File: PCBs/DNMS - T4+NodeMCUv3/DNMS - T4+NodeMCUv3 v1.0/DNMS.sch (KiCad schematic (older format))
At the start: 15 parts, among them J1 Conn_02x03_Odd_Even, J2 Conn_01x02, J3 Conn_01x04, J4 Conn_01x05, U2 NodeMCU V3, U3 Teensy4.0

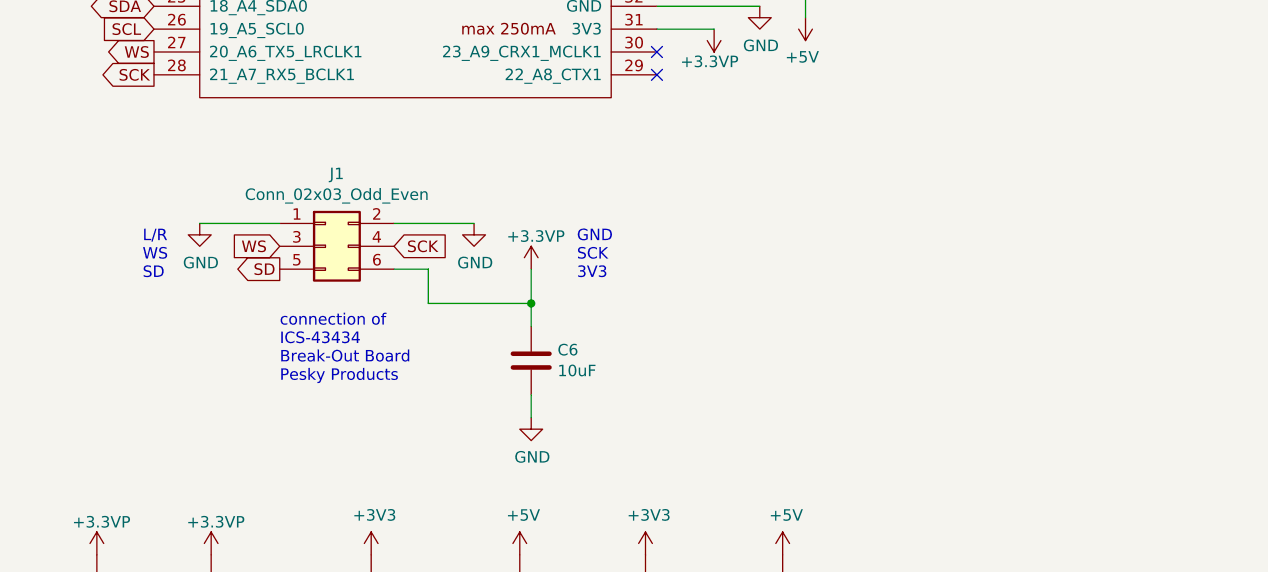
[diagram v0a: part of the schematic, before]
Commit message: change connector to mic to molex pico-ezmate
move other connectors around
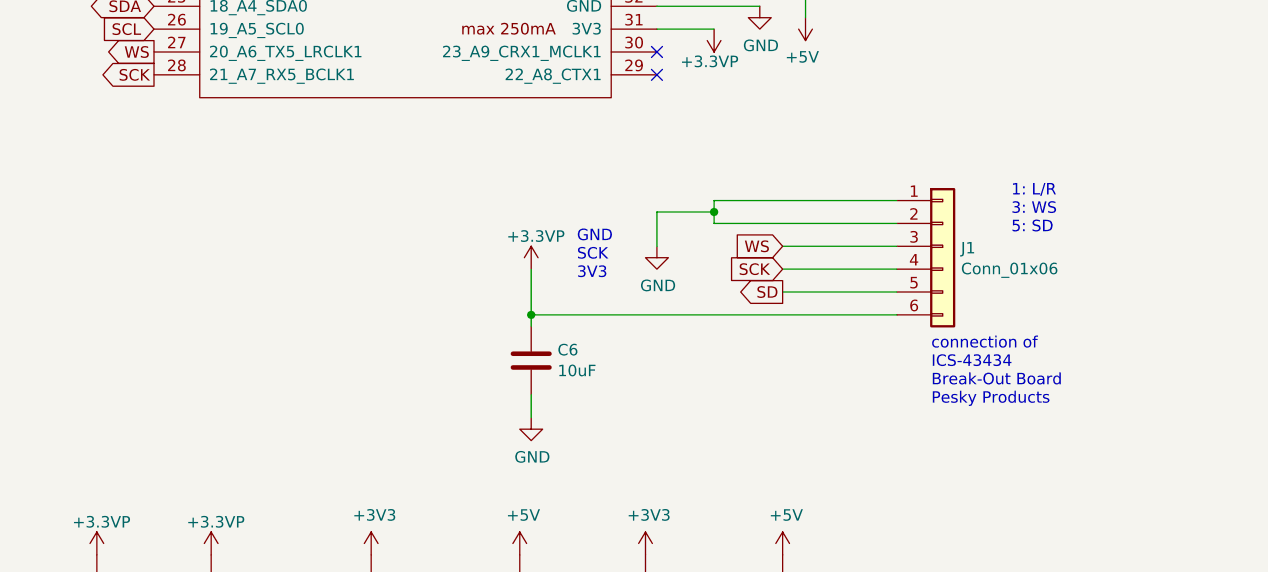
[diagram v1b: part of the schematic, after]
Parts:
- removed J1: Conn_02x03_Odd_Even, Connector_PinHeader_2.54mm:PinHeader_2x03_P2.54mm_Vertical, symbol Connector_Generic:Conn_02x03_Odd_Even
- added J1: Conn_01x06, Connector_Molex:Molex_Pico-EZmate_78171-0005_1x05-1MP_P1.20mm_Vertical, symbol Connector_Generic:Conn_01x06
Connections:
- net +3.3VP: now also J1.6 (Pin_6)
- net GND: now also J1.1 (Pin_1), J1.2 (Pin_2)
- net SCK: now also J1.4 (Pin_4)
- net SD: now also J1.5 (Pin_5)
- net WS: now also J1.3 (Pin_3)
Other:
- note added: "1: L/R\n3: WS\n5: SD"
- note removed: "L/R\nWS\nSD"
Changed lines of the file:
@@
 Text Notes 4800 3250 0    50   ~ 0
 Jumper\nVUSB nach VIN
-Text Notes 1350 4700 0    50   ~ 0
-L/R\nWS\nSD
-Text Notes 1950 5150 0    50   ~ 0
+Text Notes 5150 4500 0    50   ~ 0
+1: L/R\n3: WS\n5: SD
+Text Notes 4800 5250 0    50   ~ 0
 connection of\nICS-43434\nBreak-Out Board\nPesky Products
 Text Notes 3250 4700 0    50   ~ 0
@@
 Text GLabel 9350 4500 0    50   Input ~ 0
 SCL
-Text GLabel 1950 4550 0    50   Input ~ 0
-WS
-Text GLabel 1950 4650 0    50   Output ~ 0
-SD
-Text GLabel 2450 4550 2    50   Input ~ 0
-SCK
-Wire Wire Line
-	1950 4450 1600 4450
-Wire Wire Line
-	2450 4450 2800 4450
-$Comp
-L power:GND #PWR0126
-U 1 1 5D6C3101
-P 1600 4450
-F 0 "#PWR0126" H 1600 4200 50  0001 C CNN
-F 1 "GND" H 1605 4277 50  0000 C CNN
-F 2 "" H 1600 4450 50  0001 C CNN
-F 3 "" H 1600 4450 50  0001 C CNN
-	1    1600 4450
-	1    0    0    -1
-$EndComp
-$Comp
-L power:GND #PWR0127
-U 1 1 5D6C35EC
-P 2800 4450
-F 0 "#PWR0127" H 2800 4200 50  0001 C CNN
-F 1 "GND" H 2805 4277 50  0000 C CNN
-F 2 "" H 2800 4450 50  0001 C CNN
-F 3 "" H 2800 4450 50  0001 C CNN
-	1    2800 4450
-	1    0    0    -1
-$EndComp
-Wire Wire Line
-	2450 4650 2600 4650
-Wire Wire Line
-	2600 4650 2600 4800
-Wire Wire Line
-	2600 4800 3050 4800
-Wire Wire Line
-	3050 4800 3050 4650
 $Comp
 L power:+3.3VP #PWR0128
@@
 	10000 2700 9700 2700
 $Comp
-L Connector_Generic:Conn_02x03_Odd_Even J1
-U 1 1 5E455872
-P 2150 4550
-F 0 "J1" H 2200 4867 50  0000 C CNN
-F 1 "Conn_02x03_Odd_Even" H 2200 4776 50  0000 C CNN
-F 2 "Connector_PinHeader_2.54mm:PinHeader_2x03_P2.54mm_Vertical" H 2150 4550 50  0001 C CNN
-F 3 "~" H 2150 4550 50  0001 C CNN
-	1    2150 4550
-	1    0    0    -1
-$EndComp
-$Comp
 L Device:C C4
 U 1 1 5E4DAB70
@@
 $EndComp
 Wire Wire Line
-	3050 4900 3050 4800
-Connection ~ 3050 4800
+	3050 4900 3050 4850
 Wire Wire Line
 	3050 5200 3050 5300
@@
 	1    0    0    -1
 $EndComp
+$Comp
+L Connector_Generic:Conn_01x06 J1
+U 1 1 5E508C40
+P 4850 4550
+F 0 "J1" H 4930 4542 50  0000 L CNN
+F 1 "Conn_01x06" H 4930 4451 50  0000 L CNN
+F 2 "Connector_Molex:Molex_Pico-EZmate_78171-0005_1x05-1MP_P1.20mm_Vertical" H 4850 4550 50  0001 C CNN
+F 3 "~" H 4850 4550 50  0001 C CNN
+	1    4850 4550
+	1    0    0    -1
+$EndComp
+Wire Wire Line
+	4650 4350 3850 4350
+Wire Wire Line
+	4650 4450 3850 4450
+Wire Wire Line
+	3850 4350 3850 4400
+Wire Wire Line
+	3850 4400 3600 4400
+Wire Wire Line
+	3600 4400 3600 4550
+Connection ~ 3850 4400
+Wire Wire Line
+	3850 4400 3850 4450
+$Comp
+L power:GND #PWR0126
+U 1 1 5E512A7D
+P 3600 4550
+F 0 "#PWR0126" H 3600 4300 50  0001 C CNN
+F 1 "GND" H 3605 4377 50  0000 C CNN
+F 2 "" H 3600 4550 50  0001 C CNN
+F 3 "" H 3600 4550 50  0001 C CNN
+	1    3600 4550
+	1    0    0    -1
+$EndComp
+Wire Wire Line
+	3050 4850 4650 4850
+Connection ~ 3050 4850
+Wire Wire Line
+	4650 4550 4150 4550
+Wire Wire Line
+	4650 4650 4150 4650
+Wire Wire Line
+	4650 4750 4150 4750
+Text GLabel 4150 4550 0    50   Input ~ 0
+WS
+Text GLabel 4150 4650 0    50   Input ~ 0
+SCK
+Text GLabel 4150 4750 0    50   Output ~ 0
+SD
+Wire Wire Line
+	3050 4650 3050 4850
 $EndSCHEMATC

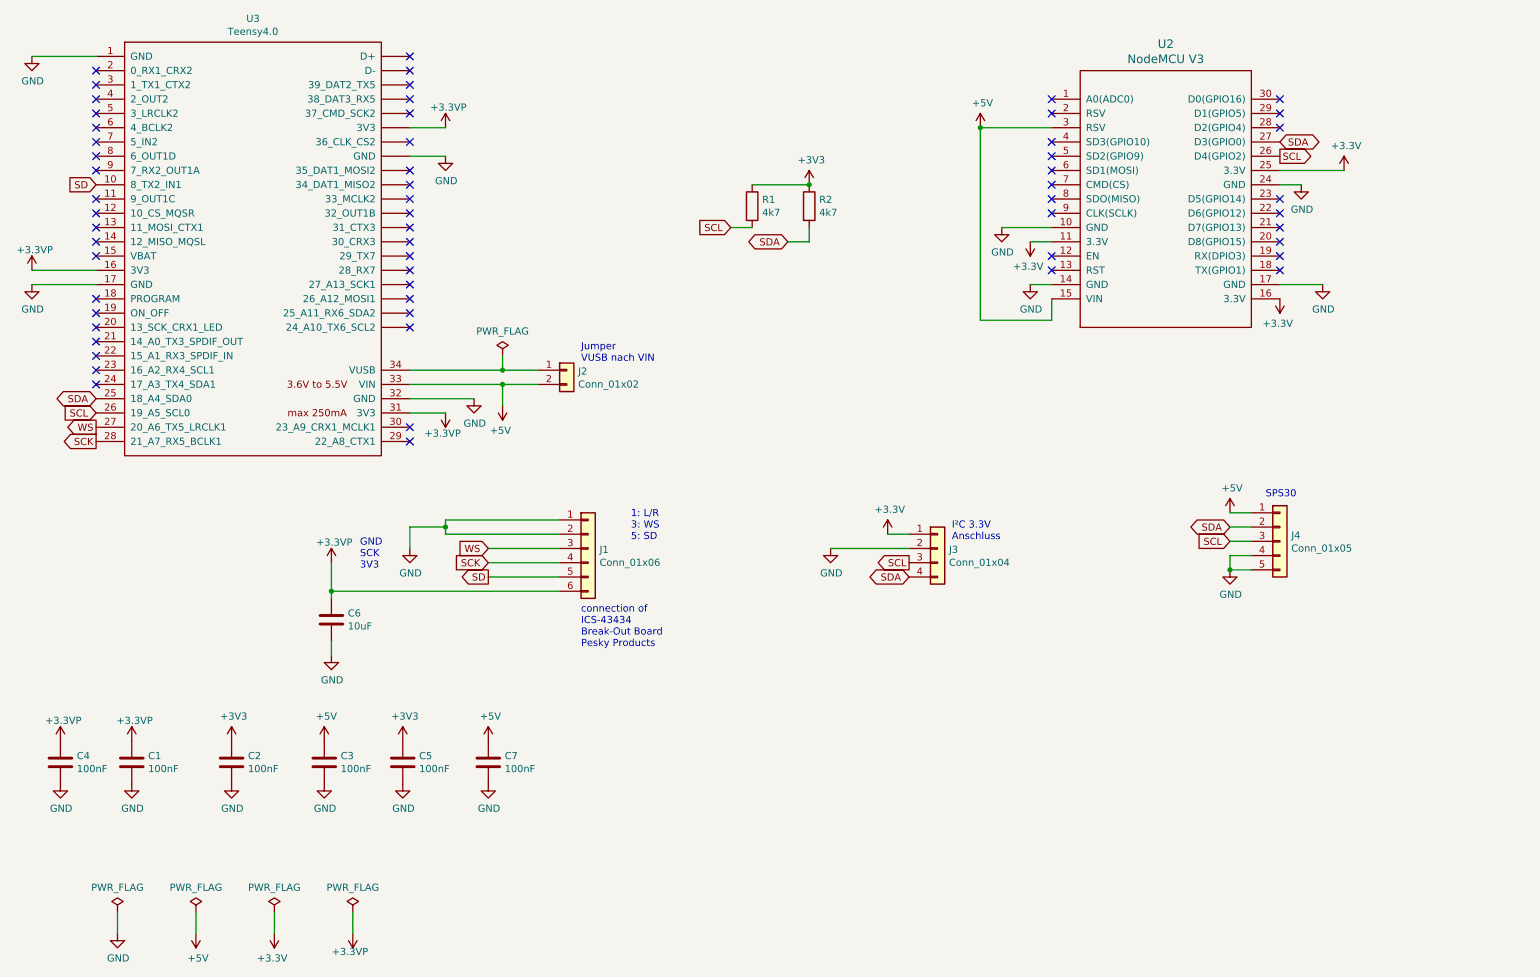
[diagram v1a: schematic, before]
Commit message: add 2.54mm connector headers next to pico ezmate connectors
for backwards compability

moved text around and cleaned design

added additional capcitors
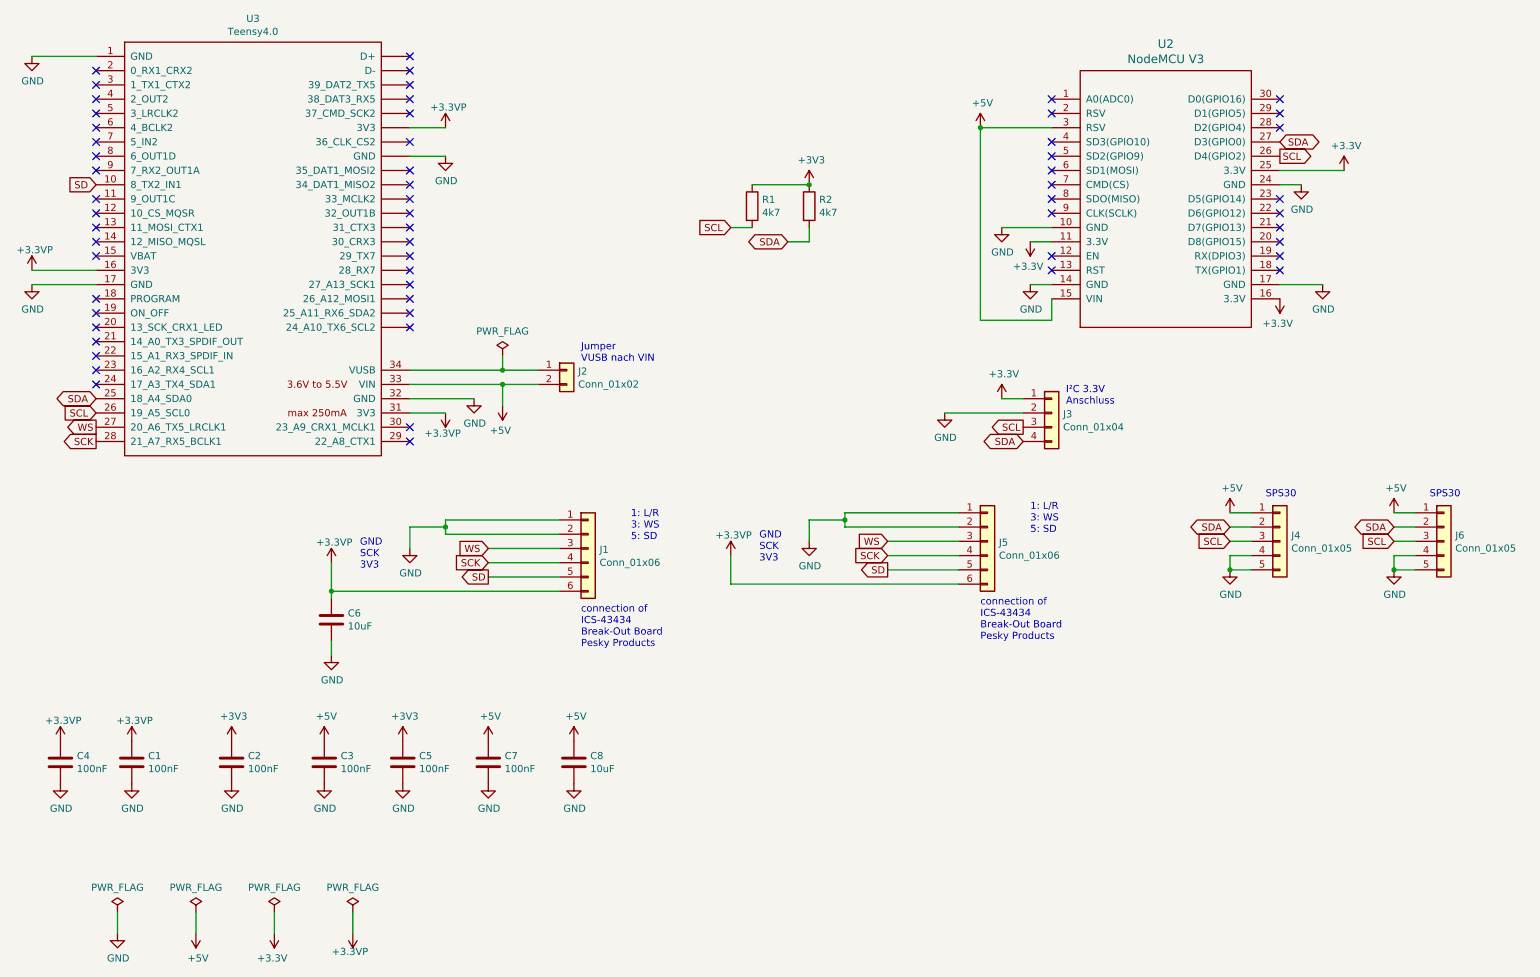
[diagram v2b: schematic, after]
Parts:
- added C8: 10uF, Capacitor_SMD:C_0805_2012Metric_Pad1.15x1.40mm_HandSolder, symbol Device:C
- added J5: Conn_01x06, Connector_PinHeader_2.54mm:PinHeader_1x06_P2.54mm_Vertical, symbol Connector_Generic:Conn_01x06
- added J6: Conn_01x05, Connector_PinHeader_2.54mm:PinHeader_1x05_P2.54mm_Vertical, symbol Connector_Generic:Conn_01x05
- J1: footprint Connector_Molex:Molex_Pico-EZmate_78171-0005_1x05-1MP_P1.20mm_Vertical -> Connector_Molex:molex_pico-ezmate_781715006_1x06_P1.20mm_Horizontal
- J4: footprint Connector_JST_ZH:JST_ZH_S5B-EH_1x05_P1.50mm_Horizontal -> Connector_Molex:Molex_Pico-EZmate_78171-0005_1x05-1MP_P1.20mm_Horizontal
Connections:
- net +3.3VP: now also J5.6 (Pin_6)
- net +5V: now also C8.1, J6.1 (Pin_1)
- net GND: now also C8.2, J5.1 (Pin_1), J5.2 (Pin_2), J6.4 (Pin_4), J6.5 (Pin_5)
- net SCK: now also J5.4 (Pin_4)
- net SCL: now also J6.3 (Pin_3)
- net SD: now also J5.5 (Pin_5)
- net SDA: now also J6.2 (Pin_2)
- net WS: now also J5.3 (Pin_3)
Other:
- moved on the sheet: J3
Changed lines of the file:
@@
 L Connector_Generic:Conn_01x04 J3
 U 1 1 5CFB9C02
-P 7300 4550
-F 0 "J3" H 7380 4542 50  0000 L CNN
-F 1 "Conn_01x04" H 7380 4451 50  0000 L CNN
-F 2 "Connector_PinHeader_2.54mm:PinHeader_1x04_P2.54mm_Vertical" H 7300 4550 50  0001 C CNN
-F 3 "~" H 7300 4550 50  0001 C CNN
-	1    7300 4550
+P 8100 3600
+F 0 "J3" H 8180 3592 50  0000 L CNN
+F 1 "Conn_01x04" H 8180 3501 50  0000 L CNN
+F 2 "Connector_PinHeader_2.54mm:PinHeader_1x04_P2.54mm_Vertical" H 8100 3600 50  0001 C CNN
+F 3 "~" H 8100 3600 50  0001 C CNN
+	1    8100 3600
 	1    0    0    -1
 $EndComp
@@
 L power:GND #PWR0105
 U 1 1 5CFBE0E7
-P 6550 4550
-F 0 "#PWR0105" H 6550 4300 50  0001 C CNN
-F 1 "GND" H 6555 4377 50  0000 C CNN
-F 2 "" H 6550 4550 50  0001 C CNN
-F 3 "" H 6550 4550 50  0001 C CNN
-	1    6550 4550
+P 7350 3600
+F 0 "#PWR0105" H 7350 3350 50  0001 C CNN
+F 1 "GND" H 7355 3427 50  0000 C CNN
+F 2 "" H 7350 3600 50  0001 C CNN
+F 3 "" H 7350 3600 50  0001 C CNN
+	1    7350 3600
 	1    0    0    -1
 $EndComp
@@
 	4250 3300 4500 3300
 Wire Wire Line
-	6950 4450 7100 4450
+	7750 3500 7900 3500
 $Comp
 L Device:C C3
@@
 Wire Wire Line
 	6400 2400 6400 2300
-Text GLabel 7100 4650 0    50   Output ~ 0
+Text GLabel 7900 3700 0    50   Output ~ 0
 SCL
-Text GLabel 7100 4750 0    50   BiDi ~ 0
+Text GLabel 7900 3800 0    50   BiDi ~ 0
 SDA
 Wire Wire Line
-	6550 4550 7100 4550
-Text Notes 7400 4500 0    50   ~ 0
+	7350 3600 7900 3600
+Text Notes 8200 3550 0    50   ~ 0
 I²C 3.3V\nAnschluss
 Text Notes 4800 3250 0    50   ~ 0
@@
 L power:+3.3V #PWR0112
 U 1 1 5D6D0B7D
-P 6950 4450
-F 0 "#PWR0112" H 6950 4300 50  0001 C CNN
-F 1 "+3.3V" H 6965 4623 50  0000 C CNN
-F 2 "" H 6950 4450 50  0001 C CNN
-F 3 "" H 6950 4450 50  0001 C CNN
-	1    6950 4450
+P 7750 3500
+F 0 "#PWR0112" H 7750 3350 50  0001 C CNN
+F 1 "+3.3V" H 7765 3673 50  0000 C CNN
+F 2 "" H 7750 3500 50  0001 C CNN
+F 3 "" H 7750 3500 50  0001 C CNN
+	1    7750 3500
 	1    0    0    -1
 $EndComp
@@
 F 0 "J4" H 9780 4542 50  0000 L CNN
 F 1 "Conn_01x05" H 9780 4451 50  0000 L CNN
-F 2 "Connector_JST_ZH:JST_ZH_S5B-EH_1x05_P1.50mm_Horizontal" H 9700 4500 50  0001 C CNN
+F 2 "Connector_Molex:Molex_Pico-EZmate_78171-0005_1x05-1MP_P1.20mm_Horizontal" H 9700 4500 50  0001 C CNN
 F 3 "~" H 9700 4500 50  0001 C CNN
 	1    9700 4500
@@
 F 0 "J1" H 4930 4542 50  0000 L CNN
 F 1 "Conn_01x06" H 4930 4451 50  0000 L CNN
-F 2 "Connector_Molex:Molex_Pico-EZmate_78171-0005_1x05-1MP_P1.20mm_Vertical" H 4850 4550 50  0001 C CNN
+F 2 "Connector_Molex:molex_pico-ezmate_781715006_1x06_P1.20mm_Horizontal" H 4850 4550 50  0001 C CNN
 F 3 "~" H 4850 4550 50  0001 C CNN
 	1    4850 4550
@@
 Wire Wire Line
 	3050 4650 3050 4850
+Text Notes 7950 4450 0    50   ~ 0
+1: L/R\n3: WS\n5: SD
+Text Notes 7600 5200 0    50   ~ 0
+connection of\nICS-43434\nBreak-Out Board\nPesky Products
+Text Notes 6050 4650 0    50   ~ 0
+GND\nSCK\n3V3
+$Comp
+L power:+3.3VP #PWR0127
+U 1 1 5E5759C8
+P 5850 4600
+F 0 "#PWR0127" H 6000 4550 50  0001 C CNN
+F 1 "+3.3VP" H 5870 4743 50  0000 C CNN
+F 2 "" H 5850 4600 50  0001 C CNN
+F 3 "" H 5850 4600 50  0001 C CNN
+	1    5850 4600
+	1    0    0    -1
+$EndComp
+$Comp
+L Connector_Generic:Conn_01x06 J5
+U 1 1 5E5759DC
+P 7650 4500
+F 0 "J5" H 7730 4492 50  0000 L CNN
+F 1 "Conn_01x06" H 7730 4401 50  0000 L CNN
+F 2 "Connector_PinHeader_2.54mm:PinHeader_1x06_P2.54mm_Vertical" H 7650 4500 50  0001 C CNN
+F 3 "~" H 7650 4500 50  0001 C CNN
+	1    7650 4500
+	1    0    0    -1
+$EndComp
+Wire Wire Line
+	7450 4300 6650 4300
+Wire Wire Line
+	7450 4400 6650 4400
+Wire Wire Line
+	6650 4300 6650 4350
+Wire Wire Line
+	6650 4350 6400 4350
+Wire Wire Line
+	6400 4350 6400 4500
+Connection ~ 6650 4350
+Wire Wire Line
+	6650 4350 6650 4400
+$Comp
+L power:GND #PWR0143
+U 1 1 5E5759E9
+P 6400 4500
+F 0 "#PWR0143" H 6400 4250 50  0001 C CNN
+F 1 "GND" H 6405 4327 50  0000 C CNN
+F 2 "" H 6400 4500 50  0001 C CNN
+F 3 "" H 6400 4500 50  0001 C CNN
+	1    6400 4500
+	1    0    0    -1
+$EndComp
+Wire Wire Line
+	5850 4800 7450 4800
+Wire Wire Line
+	7450 4500 6950 4500
+Wire Wire Line
+	7450 4600 6950 4600
+Wire Wire Line
+	7450 4700 6950 4700
+Text GLabel 6950 4500 0    50   Input ~ 0
+WS
+Text GLabel 6950 4600 0    50   Input ~ 0
+SCK
+Text GLabel 6950 4700 0    50   Output ~ 0
+SD
+Wire Wire Line
+	5850 4600 5850 4800
+Text Notes 10750 4200 0    50   ~ 0
+SPS30
+Wire Wire Line
+	10650 4300 10500 4300
+Wire Wire Line
+	10650 4400 10500 4400
+Wire Wire Line
+	10650 4500 10500 4500
+Wire Wire Line
+	10650 4600 10500 4600
+Wire Wire Line
+	10650 4700 10500 4700
+Wire Wire Line
+	10500 4600 10500 4700
+$Comp
+L power:GND #PWR0142
+U 1 1 5E58E44B
+P 10500 4700
+F 0 "#PWR0142" H 10500 4450 50  0001 C CNN
+F 1 "GND" H 10505 4527 50  0000 C CNN
+F 2 "" H 10500 4700 50  0001 C CNN
+F 3 "" H 10500 4700 50  0001 C CNN
+	1    10500 4700
+	1    0    0    -1
+$EndComp
+Connection ~ 10500 4700
+$Comp
+L power:+5V #PWR0144
+U 1 1 5E58E452
+P 10500 4300
+F 0 "#PWR0144" H 10500 4150 50  0001 C CNN
+F 1 "+5V" H 10515 4473 50  0000 C CNN
+F 2 "" H 10500 4300 50  0001 C CNN
+F 3 "" H 10500 4300 50  0001 C CNN
+	1    10500 4300
+	1    0    0    -1
+$EndComp
+Text GLabel 10500 4400 0    50   BiDi ~ 0
+SDA
+$Comp
+L Connector_Generic:Conn_01x05 J6
+U 1 1 5E58E459
+P 10850 4500
+F 0 "J6" H 10930 4542 50  0000 L CNN
+F 1 "Conn_01x05" H 10930 4451 50  0000 L CNN
+F 2 "Connector_PinHeader_2.54mm:PinHeader_1x05_P2.54mm_Vertical" H 10850 4500 50  0001 C CNN
+F 3 "~" H 10850 4500 50  0001 C CNN
+	1    10850 4500
+	1    0    0    -1
+$EndComp
+Text GLabel 10500 4500 0    50   Input ~ 0
+SCL
+$Comp
+L Device:C C8
+U 1 1 5E578EF7
+P 4750 6050
+F 0 "C8" H 4865 6096 50  0000 L CNN
+F 1 "10uF" H 4865 6005 50  0000 L CNN
+F 2 "Capacitor_SMD:C_0805_2012Metric_Pad1.15x1.40mm_HandSolder" H 4788 5900 50  0001 C CNN
+F 3 "~" H 4750 6050 50  0001 C CNN
+	1    4750 6050
+	1    0    0    -1
+$EndComp
+$Comp
+L power:GND #PWR0145
+U 1 1 5E578EFD
+P 4750 6200
+F 0 "#PWR0145" H 4750 5950 50  0001 C CNN
+F 1 "GND" H 4755 6027 50  0000 C CNN
+F 2 "" H 4750 6200 50  0001 C CNN
+F 3 "" H 4750 6200 50  0001 C CNN
+	1    4750 6200
+	1    0    0    -1
+$EndComp
+$Comp
+L power:+5V #PWR0146
+U 1 1 5E578F03
+P 4750 5900
+F 0 "#PWR0146" H 4750 5750 50  0001 C CNN
+F 1 "+5V" H 4765 6073 50  0000 C CNN
+F 2 "" H 4750 5900 50  0001 C CNN
+F 3 "" H 4750 5900 50  0001 C CNN
+	1    4750 5900
+	1    0    0    -1
+$EndComp
 $EndSCHEMATC
